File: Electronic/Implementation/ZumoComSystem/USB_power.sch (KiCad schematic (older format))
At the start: 1 part, among them P1 USB_C_Plug

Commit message: electronic -> Schematic -> add hierarchical pins, modified Regulator page
           -> BOM & Clac: add new inductors
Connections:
- net labels added: D+, D-, V_Bat
- wire segments 0 -> 2
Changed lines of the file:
@@
 L Connector:USB_C_Plug P?
 U 1 1 60C67689
-P 1400 2100
+P 1900 2100
 AR Path="/60C67689" Ref="P?"  Part="1"
 AR Path="/60C3F428/60C67689" Ref="P1"  Part="1"
-F 0 "P1" H 1507 3367 50  0000 C CNN
-F 1 "USB_C_Plug" H 1507 3276 50  0000 C CNN
-F 2 "footprints:USB_C_Receptacle_JAE_DX07S024WJ3R400" H 1550 2100 50  0001 C CNN
-F 3 "https://www.usb.org/sites/default/files/documents/usb_type-c.zip" H 1550 2100 50  0001 C CNN
-	1    1400 2100
+F 0 "P1" H 2007 3367 50  0000 C CNN
+F 1 "USB_C_Plug" H 2007 3276 50  0000 C CNN
+F 2 "footprints:USB_C_Receptacle_JAE_DX07S024WJ3R400" H 2050 2100 50  0001 C CNN
+F 3 "https://www.usb.org/sites/default/files/documents/usb_type-c.zip" H 2050 2100 50  0001 C CNN
+	1    1900 2100
 	1    0    0    -1
 $EndComp
+Text HLabel 1100 4400 0    50   Input ~ 0
+V_Bat
+Text HLabel 3050 1600 2    50   Output ~ 0
+D-
+Text HLabel 3050 1800 2    50   Output ~ 0
+D+
+Wire Wire Line
+	2500 1600 3050 1600
+Wire Wire Line
+	2500 1800 3050 1800
 $EndSCHEMATC

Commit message: Electronic: Schematic: ESP I/Os, IF_Pololu Pins, USB_max
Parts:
- removed P1: USB_C_Plug, footprints:USB_C_Receptacle_JAE_DX07S024WJ3R400, symbol Connector:USB_C_Plug
- added J2: USB_B_Micro, footprints:USB_Micro-B_Molex-105133-0001-3D, symbol Connector:USB_B_Micro
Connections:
- net labels added: GND
- wire segments 2 -> 10
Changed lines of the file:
@@
 $Descr A4 11693 8268
 encoding utf-8
-Sheet 4 7
+Sheet 5 7
 Title "Zumo Communication System"
-Date "2021-06-11"
+Date "2021-07-28"
 Rev "V1.0"
 Comp "NewTec GmbH"
@@
 Comment4 ""
 $EndDescr
+Text HLabel 2850 1450 2    50   Output ~ 0
+V_Bat
+Text HLabel 2850 1750 2    50   BiDi ~ 0
+D-
+Text HLabel 2850 1650 2    50   BiDi ~ 0
+D+
+Wire Wire Line
+	2300 1750 2850 1750
+Wire Wire Line
+	2300 1650 2850 1650
 $Comp
-L Connector:USB_C_Plug P?
-U 1 1 60C67689
-P 1900 2100
-AR Path="/60C67689" Ref="P?"  Part="1"
-AR Path="/60C3F428/60C67689" Ref="P1"  Part="1"
-F 0 "P1" H 2007 3367 50  0000 C CNN
-F 1 "USB_C_Plug" H 2007 3276 50  0000 C CNN
-F 2 "footprints:USB_C_Receptacle_JAE_DX07S024WJ3R400" H 2050 2100 50  0001 C CNN
-F 3 "https://www.usb.org/sites/default/files/documents/usb_type-c.zip" H 2050 2100 50  0001 C CNN
-	1    1900 2100
+L Connector:USB_B_Micro J2
+U 1 1 60DEC307
+P 2000 1650
+F 0 "J2" H 2057 2117 50  0000 C CNN
+F 1 "USB_B_Micro" H 2057 2026 50  0000 C CNN
+F 2 "footprints:USB_Micro-B_Molex-105133-0001-3D" H 2150 1600 50  0001 C CNN
+F 3 "~" H 2150 1600 50  0001 C CNN
+	1    2000 1650
 	1    0    0    -1
 $EndComp
-Text HLabel 1100 4400 0    50   Input ~ 0
-V_Bat
-Text HLabel 3050 1600 2    50   Output ~ 0
-D-
-Text HLabel 3050 1800 2    50   Output ~ 0
-D+
 Wire Wire Line
-	2500 1600 3050 1600
+	2850 1450 2300 1450
 Wire Wire Line
-	2500 1800 3050 1800
+	1900 2050 1900 2150
+Wire Wire Line
+	2000 2150 2000 2050
+Wire Wire Line
+	2000 2150 2000 2250
+$Comp
+L power:GND #PWR020
+U 1 1 60DEDA4E
+P 2000 2250
+F 0 "#PWR020" H 2000 2000 50  0001 C CNN
+F 1 "GND" H 2005 2077 50  0000 C CNN
+F 2 "" H 2000 2250 50  0001 C CNN
+F 3 "" H 2000 2250 50  0001 C CNN
+	1    2000 2250
+	1    0    0    -1
+$EndComp
+Wire Wire Line
+	2000 2150 2350 2150
+Wire Wire Line
+	2350 2150 2350 1850
+Wire Wire Line
+	2350 1850 2300 1850
+Connection ~ 2000 2150
+Wire Wire Line
+	1900 2150 2000 2150
 $EndSCHEMATC

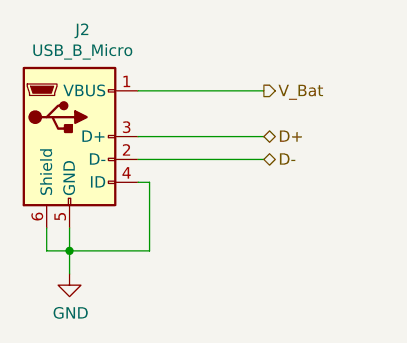
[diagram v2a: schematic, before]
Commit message: electronic: BOM: n-mosfet; SMD-pin correct position
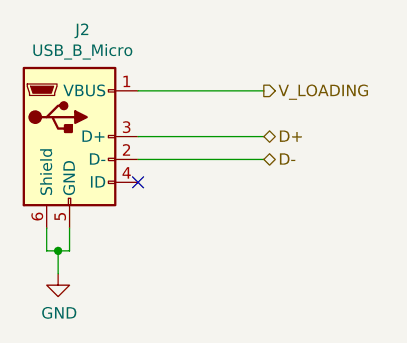
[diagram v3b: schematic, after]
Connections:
- net GND: no longer J2.4 (ID)
- net V_Bat renamed V_LOADING
- no-connect marks 0 -> 1
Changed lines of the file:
@@
 Sheet 5 7
 Title "Zumo Communication System"
-Date "2021-07-28"
+Date "2021-07-30"
 Rev "V1.0"
 Comp "NewTec GmbH"
 Comment1 "Schneider, Niklas"
-Comment2 "Schneider, Niklas"
+Comment2 ""
 Comment3 ""
 Comment4 ""
 $EndDescr
 Text HLabel 2850 1450 2    50   Output ~ 0
-V_Bat
+V_LOADING
 Text HLabel 2850 1750 2    50   BiDi ~ 0
 D-
@@
 	2000 2150 2000 2050
 Wire Wire Line
-	2000 2150 2000 2250
+	1950 2150 1950 2250
 $Comp
 L power:GND #PWR020
 U 1 1 60DEDA4E
-P 2000 2250
-F 0 "#PWR020" H 2000 2000 50  0001 C CNN
-F 1 "GND" H 2005 2077 50  0000 C CNN
-F 2 "" H 2000 2250 50  0001 C CNN
-F 3 "" H 2000 2250 50  0001 C CNN
-	1    2000 2250
+P 1950 2250
+F 0 "#PWR020" H 1950 2000 50  0001 C CNN
+F 1 "GND" H 1955 2077 50  0000 C CNN
+F 2 "" H 1950 2250 50  0001 C CNN
+F 3 "" H 1950 2250 50  0001 C CNN
+	1    1950 2250
 	1    0    0    -1
 $EndComp
 Wire Wire Line
-	2000 2150 2350 2150
+	1900 2150 1950 2150
+Connection ~ 1950 2150
 Wire Wire Line
-	2350 2150 2350 1850
-Wire Wire Line
-	2350 1850 2300 1850
-Connection ~ 2000 2150
-Wire Wire Line
-	1900 2150 2000 2150
+	1950 2150 2000 2150
+NoConn ~ 2300 1850
 $EndSCHEMATC

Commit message: add charger
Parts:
- added C?: 22uF, Capacitor_SMD:C_1206_3216Metric_Pad1.42x1.75mm_HandSolder, symbol Device:C
- added C?: 220n, symbol Device:C
- added R?: 10k, symbol Device:R
- added R?: 10, symbol Device:R
- added U?: R1218N021A, Package_TO_SOT_SMD:SOT-23-6_Handsoldering, symbol LT1374CS8-5PBF:R1218N021A
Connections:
- net GND: now also C?.2, R?.2, U?.5 (GND)
- net V_LOADING: now also C?.1, U?.2 (VOUT); no longer J2.1 (VBUS)
- new net: R?.1, U?.1 (CE)
- new net: C?.2, U?.4 (Lx)
- new net: R?.1, U?.6 (VFB)
- new net V_USB_Bat: C?.1, J2.1 (VBUS), R?.2, U?.3 (VIN)
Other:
- note added: "V_Loading = 8.5V"
- moved on the sheet: J2
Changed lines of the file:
@@
 Comment4 ""
 $EndDescr
-Text HLabel 2850 1450 2    50   Output ~ 0
+Text HLabel 6000 2350 0    50   Output ~ 0
 V_LOADING
-Text HLabel 2850 1750 2    50   BiDi ~ 0
+Text HLabel 3150 3300 2    50   BiDi ~ 0
 D-
-Text HLabel 2850 1650 2    50   BiDi ~ 0
+Text HLabel 3150 3200 2    50   BiDi ~ 0
 D+
 Wire Wire Line
-	2300 1750 2850 1750
+	2800 3300 3150 3300
 Wire Wire Line
-	2300 1650 2850 1650
+	2800 3200 3150 3200
 $Comp
 L Connector:USB_B_Micro J2
 U 1 1 60DEC307
-P 2000 1650
-F 0 "J2" H 2057 2117 50  0000 C CNN
-F 1 "USB_B_Micro" H 2057 2026 50  0000 C CNN
-F 2 "footprints:USB_Micro-B_Molex-105133-0001-3D" H 2150 1600 50  0001 C CNN
-F 3 "~" H 2150 1600 50  0001 C CNN
-	1    2000 1650
+P 2500 3200
+F 0 "J2" H 2557 3667 50  0000 C CNN
+F 1 "USB_B_Micro" H 2557 3576 50  0000 C CNN
+F 2 "footprints:USB_Micro-B_Molex-105133-0001-3D" H 2650 3150 50  0001 C CNN
+F 3 "~" H 2650 3150 50  0001 C CNN
+	1    2500 3200
 	1    0    0    -1
 $EndComp
 Wire Wire Line
-	2850 1450 2300 1450
+	2400 3600 2400 3700
 Wire Wire Line
-	1900 2050 1900 2150
+	2500 3700 2500 3600
 Wire Wire Line
-	2000 2150 2000 2050
-Wire Wire Line
-	1950 2150 1950 2250
+	2450 3700 2450 3800
 $Comp
 L power:GND #PWR020
 U 1 1 60DEDA4E
-P 1950 2250
-F 0 "#PWR020" H 1950 2000 50  0001 C CNN
-F 1 "GND" H 1955 2077 50  0000 C CNN
-F 2 "" H 1950 2250 50  0001 C CNN
-F 3 "" H 1950 2250 50  0001 C CNN
-	1    1950 2250
+P 2450 3800
+F 0 "#PWR020" H 2450 3550 50  0001 C CNN
+F 1 "GND" H 2455 3627 50  0000 C CNN
+F 2 "" H 2450 3800 50  0001 C CNN
+F 3 "" H 2450 3800 50  0001 C CNN
+	1    2450 3800
 	1    0    0    -1
 $EndComp
 Wire Wire Line
-	1900 2150 1950 2150
-Connection ~ 1950 2150
+	2400 3700 2450 3700
+Connection ~ 2450 3700
 Wire Wire Line
-	1950 2150 2000 2150
-NoConn ~ 2300 1850
+	2450 3700 2500 3700
+NoConn ~ 2800 3400
+$Comp
+L LT1374CS8-5PBF:R1218N021A U?
+U 1 1 621F5235
+P 7300 2350
+F 0 "U?" H 7300 2765 50  0000 C CNN
+F 1 "R1218N021A" H 7300 2674 50  0000 C CNN
+F 2 "Package_TO_SOT_SMD:SOT-23-6_Handsoldering" H 7700 2700 50  0001 C CNN
+F 3 "https://www.nisshinbo-microdevices.co.jp/en/pdf/datasheet/r1218-ea.pdf" H 7700 2700 50  0001 C CNN
+	1    7300 2350
+	1    0    0    -1
+$EndComp
+Wire Wire Line
+	7650 2350 8100 2350
+Wire Wire Line
+	8100 2350 8100 2750
+$Comp
+L power:GND #PWR?
+U 1 1 621F66D3
+P 8100 2750
+F 0 "#PWR?" H 8100 2500 50  0001 C CNN
+F 1 "GND" H 8105 2577 50  0000 C CNN
+F 2 "" H 8100 2750 50  0001 C CNN
+F 3 "" H 8100 2750 50  0001 C CNN
+	1    8100 2750
+	1    0    0    -1
+$EndComp
+Wire Wire Line
+	6950 2350 6250 2350
+Wire Wire Line
+	6950 2200 5800 2200
+Wire Wire Line
+	5000 3000 6800 3000
+$Comp
+L Device:R R?
+U 1 1 621FAFF2
+P 5650 2200
+F 0 "R?" V 5443 2200 50  0000 C CNN
+F 1 "10k" V 5534 2200 50  0000 C CNN
+F 2 "" V 5580 2200 50  0001 C CNN
+F 3 "~" H 5650 2200 50  0001 C CNN
+	1    5650 2200
+	0    1    1    0
+$EndComp
+Wire Wire Line
+	5500 2200 5000 2200
+$Comp
+L Device:R R?
+U 1 1 621FB991
+P 8500 2500
+F 0 "R?" H 8570 2546 50  0000 L CNN
+F 1 "10" H 8570 2455 50  0000 L CNN
+F 2 "" V 8430 2500 50  0001 C CNN
+F 3 "~" H 8500 2500 50  0001 C CNN
+	1    8500 2500
+	1    0    0    -1
+$EndComp
+Wire Wire Line
+	7650 2200 8500 2200
+$Comp
+L Device:C C?
+U 1 1 621FD3F7
+P 7300 3000
+F 0 "C?" V 7500 2950 50  0000 L CNN
+F 1 "22uF" V 7100 2900 50  0000 L CNN
+F 2 "Capacitor_SMD:C_1206_3216Metric_Pad1.42x1.75mm_HandSolder" H 7338 2850 50  0001 C CNN
+F 3 "https://product.tdk.com/info/en/catalog/datasheets/mlcc_commercial_general_en.pdf?ref_disty=digikey" H 7300 3000 50  0001 C CNN
+	1    7300 3000
+	0    -1   -1   0
+$EndComp
+Wire Wire Line
+	6800 2500 6800 3000
+Wire Wire Line
+	6800 3000 7150 3000
+Wire Wire Line
+	6800 2500 6950 2500
+Wire Wire Line
+	7450 3000 7800 3000
+Wire Wire Line
+	7800 3000 7800 2500
+Wire Wire Line
+	7800 2500 7650 2500
+Wire Wire Line
+	8500 2650 8500 2750
+$Comp
+L power:GND #PWR?
+U 1 1 621FE4AA
+P 8500 2750
+F 0 "#PWR?" H 8500 2500 50  0001 C CNN
+F 1 "GND" H 8505 2577 50  0000 C CNN
+F 2 "" H 8500 2750 50  0001 C CNN
+F 3 "" H 8500 2750 50  0001 C CNN
+	1    8500 2750
+	1    0    0    -1
+$EndComp
+Wire Wire Line
+	8500 2200 8500 2350
+Text Label 4150 3000 0    50   ~ 0
+V_USB_Bat
+Wire Wire Line
+	2800 3000 5000 3000
+Connection ~ 5000 3000
+Connection ~ 6800 3000
+Wire Wire Line
+	5000 2200 5000 3000
+$Comp
+L Device:C C?
+U 1 1 62201332
+P 6250 2550
+F 0 "C?" H 6365 2596 50  0000 L CNN
+F 1 "220n" H 6365 2505 50  0000 L CNN
+F 2 "" H 6288 2400 50  0001 C CNN
+F 3 "~" H 6250 2550 50  0001 C CNN
+	1    6250 2550
+	1    0    0    -1
+$EndComp
+Wire Wire Line
+	6250 2700 6250 2750
+Wire Wire Line
+	6250 2400 6250 2350
+Connection ~ 6250 2350
+Wire Wire Line
+	6250 2350 6000 2350
+$Comp
+L power:GND #PWR?
+U 1 1 62201F1D
+P 6250 2750
+F 0 "#PWR?" H 6250 2500 50  0001 C CNN
+F 1 "GND" H 6255 2577 50  0000 C CNN
+F 2 "" H 6250 2750 50  0001 C CNN
+F 3 "" H 6250 2750 50  0001 C CNN
+	1    6250 2750
+	1    0    0    -1
+$EndComp
+Text Notes 6950 1750 0    50   ~ 0
+V_Loading = 8.5V
 $EndSCHEMATC

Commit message: Electronic: no charger, added Cp2102 instead of Ft232, first palcement
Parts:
- removed C?: 22uF, Capacitor_SMD:C_1206_3216Metric_Pad1.42x1.75mm_HandSolder, symbol Device:C
- added D6, D7, D8: D5V0S1U2WS-7, Diode_SMD:D_SOD-323_HandSoldering, symbol Device:D
- added L3: 22uH, footprints:L_Wuerth_HCI-1350_3D, symbol Device:L
- C14: renamed from C?; footprint (none) -> Capacitor_SMD:C_0603_1608Metric_Pad1.05x0.95mm_HandSolder
- R10, R11: renamed from R?; footprint (none) -> Resistor_SMD:R_0603_1608Metric_Pad1.05x0.95mm_HandSolder
- gave numbers to parts that had none: 1
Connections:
- net D+: now also D7.1 (K)
- net D-: now also D8.1 (K)
- net GND: now also D6.2 (A), D7.2 (A), D8.2 (A)
- net at U6.4 (Lx): now also L3.2
- net V_USB_Bat renamed VBUS
- net VBUS: now also D6.1 (K), L3.1
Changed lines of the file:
@@
 Sheet 5 7
 Title "Zumo Communication System"
-Date "2021-08-20"
+Date "2022-03-08"
 Rev "V1.0"
 Comp "NewTec GmbH"
@@
 Text HLabel 6000 2350 0    50   Output ~ 0
 V_LOADING
-Text HLabel 3150 3300 2    50   BiDi ~ 0
+Text HLabel 4450 3300 2    50   BiDi ~ 0
 D-
-Text HLabel 3150 3200 2    50   BiDi ~ 0
+Text HLabel 4450 3200 2    50   BiDi ~ 0
 D+
 Wire Wire Line
-	2800 3300 3150 3300
-Wire Wire Line
-	2800 3200 3150 3200
+	2800 3300 3800 3300
+Wire Wire Line
+	2800 3200 3450 3200
 $Comp
 L Connector:USB_B_Micro J2
@@
 	2500 3700 2500 3600
 Wire Wire Line
-	2450 3700 2450 3800
-$Comp
-L power:GND #PWR020
+	2450 3700 2450 3950
+$Comp
+L power:GND #PWR030
 U 1 1 60DEDA4E
-P 2450 3800
-F 0 "#PWR020" H 2450 3550 50  0001 C CNN
-F 1 "GND" H 2455 3627 50  0000 C CNN
-F 2 "" H 2450 3800 50  0001 C CNN
-F 3 "" H 2450 3800 50  0001 C CNN
-	1    2450 3800
+P 2450 3950
+F 0 "#PWR030" H 2450 3700 50  0001 C CNN
+F 1 "GND" H 2455 3777 50  0000 C CNN
+F 2 "" H 2450 3950 50  0001 C CNN
+F 3 "" H 2450 3950 50  0001 C CNN
+	1    2450 3950
 	1    0    0    -1
 $EndComp
@@
 NoConn ~ 2800 3400
 $Comp
-L LT1374CS8-5PBF:R1218N021A U?
+L LT1374CS8-5PBF:R1218N021A U6
 U 1 1 621F5235
 P 7300 2350
-F 0 "U?" H 7300 2765 50  0000 C CNN
+F 0 "U6" H 7300 2765 50  0000 C CNN
 F 1 "R1218N021A" H 7300 2674 50  0000 C CNN
 F 2 "Package_TO_SOT_SMD:SOT-23-6_Handsoldering" H 7700 2700 50  0001 C CNN
@@
 	8100 2350 8100 2750
 $Comp
-L power:GND #PWR?
+L power:GND #PWR034
 U 1 1 621F66D3
 P 8100 2750
-F 0 "#PWR?" H 8100 2500 50  0001 C CNN
+F 0 "#PWR034" H 8100 2500 50  0001 C CNN
 F 1 "GND" H 8105 2577 50  0000 C CNN
 F 2 "" H 8100 2750 50  0001 C CNN
@@
 	5000 3000 6800 3000
 $Comp
-L Device:R R?
+L Device:R R10
 U 1 1 621FAFF2
 P 5650 2200
-F 0 "R?" V 5443 2200 50  0000 C CNN
+F 0 "R10" V 5443 2200 50  0000 C CNN
 F 1 "10k" V 5534 2200 50  0000 C CNN
-F 2 "" V 5580 2200 50  0001 C CNN
+F 2 "Resistor_SMD:R_0603_1608Metric_Pad1.05x0.95mm_HandSolder" V 5580 2200 50  0001 C CNN
 F 3 "~" H 5650 2200 50  0001 C CNN
 	1    5650 2200
@@
 	5500 2200 5000 2200
 $Comp
-L Device:R R?
+L Device:R R11
 U 1 1 621FB991
 P 8500 2500
-F 0 "R?" H 8570 2546 50  0000 L CNN
+F 0 "R11" H 8570 2546 50  0000 L CNN
 F 1 "10" H 8570 2455 50  0000 L CNN
-F 2 "" V 8430 2500 50  0001 C CNN
+F 2 "Resistor_SMD:R_0603_1608Metric_Pad1.05x0.95mm_HandSolder" V 8430 2500 50  0001 C CNN
 F 3 "~" H 8500 2500 50  0001 C CNN
 	1    8500 2500
@@
 Wire Wire Line
 	7650 2200 8500 2200
-$Comp
-L Device:C C?
-U 1 1 621FD3F7
-P 7300 3000
-F 0 "C?" V 7500 2950 50  0000 L CNN
-F 1 "22uF" V 7100 2900 50  0000 L CNN
-F 2 "Capacitor_SMD:C_1206_3216Metric_Pad1.42x1.75mm_HandSolder" H 7338 2850 50  0001 C CNN
-F 3 "https://product.tdk.com/info/en/catalog/datasheets/mlcc_commercial_general_en.pdf?ref_disty=digikey" H 7300 3000 50  0001 C CNN
-	1    7300 3000
-	0    -1   -1   0
-$EndComp
 Wire Wire Line
 	6800 2500 6800 3000
@@
 	8500 2650 8500 2750
 $Comp
-L power:GND #PWR?
+L power:GND #PWR035
 U 1 1 621FE4AA
 P 8500 2750
-F 0 "#PWR?" H 8500 2500 50  0001 C CNN
+F 0 "#PWR035" H 8500 2500 50  0001 C CNN
 F 1 "GND" H 8505 2577 50  0000 C CNN
 F 2 "" H 8500 2750 50  0001 C CNN
@@
 Wire Wire Line
 	8500 2200 8500 2350
-Text Label 4150 3000 0    50   ~ 0
-V_USB_Bat
-Wire Wire Line
-	2800 3000 5000 3000
 Connection ~ 5000 3000
 Connection ~ 6800 3000
@@
 	5000 2200 5000 3000
 $Comp
-L Device:C C?
+L Device:C C14
 U 1 1 62201332
 P 6250 2550
-F 0 "C?" H 6365 2596 50  0000 L CNN
+F 0 "C14" H 6365 2596 50  0000 L CNN
 F 1 "220n" H 6365 2505 50  0000 L CNN
-F 2 "" H 6288 2400 50  0001 C CNN
+F 2 "Capacitor_SMD:C_0603_1608Metric_Pad1.05x0.95mm_HandSolder" H 6288 2400 50  0001 C CNN
 F 3 "~" H 6250 2550 50  0001 C CNN
 	1    6250 2550
@@
 	6250 2350 6000 2350
 $Comp
-L power:GND #PWR?
+L power:GND #PWR033
 U 1 1 62201F1D
 P 6250 2750
-F 0 "#PWR?" H 6250 2500 50  0001 C CNN
+F 0 "#PWR033" H 6250 2500 50  0001 C CNN
 F 1 "GND" H 6255 2577 50  0000 C CNN
 F 2 "" H 6250 2750 50  0001 C CNN
@@
 Text Notes 6950 1750 0    50   ~ 0
 V_Loading = 8.5V
+$Comp
+L power:VBUS #PWR031
+U 1 1 6230EF27
+P 3150 2700
+F 0 "#PWR031" H 3150 2550 50  0001 C CNN
+F 1 "VBUS" H 3165 2873 50  0000 C CNN
+F 2 "" H 3150 2700 50  0001 C CNN
+F 3 "" H 3150 2700 50  0001 C CNN
+	1    3150 2700
+	1    0    0    -1
+$EndComp
+Wire Wire Line
+	3150 2700 3150 3000
+Wire Wire Line
+	2800 3000 3150 3000
+Connection ~ 3150 3000
+Wire Wire Line
+	3150 3000 5000 3000
+$Comp
+L Device:D D7
+U 1 1 6235853C
+P 3450 3600
+F 0 "D7" V 3450 3680 50  0000 L CNN
+F 1 "D5V0S1U2WS-7" V 3495 3680 50  0001 L CNN
+F 2 "Diode_SMD:D_SOD-323_HandSoldering" H 3450 3600 50  0001 C CNN
+F 3 "https://www.diodes.com/assets/Datasheets/D5V0S1U2WS.pdf" H 3450 3600 50  0001 C CNN
+	1    3450 3600
+	0    1    1    0
+$EndComp
+$Comp
+L Device:D D8
+U 1 1 62358EEE
+P 3800 3600
+F 0 "D8" V 3754 3680 50  0000 L CNN
+F 1 "D5V0S1U2WS-7" V 3800 4000 50  0000 L CNN
+F 2 "Diode_SMD:D_SOD-323_HandSoldering" H 3800 3600 50  0001 C CNN
+F 3 "https://www.diodes.com/assets/Datasheets/D5V0S1U2WS.pdf" H 3800 3600 50  0001 C CNN
+	1    3800 3600
+	0    1    1    0
+$EndComp
+Wire Wire Line
+	3450 3450 3450 3200
+Connection ~ 3450 3200
+Wire Wire Line
+	3450 3200 4450 3200
+Wire Wire Line
+	3800 3450 3800 3300
+Connection ~ 3800 3300
+Wire Wire Line
+	3800 3300 4450 3300
+$Comp
+L Device:D D6
+U 1 1 62359ADA
+P 3150 3600
+F 0 "D6" V 3150 3680 50  0000 L CNN
+F 1 "D5V0S1U2WS-7" V 3195 3680 50  0001 L CNN
+F 2 "Diode_SMD:D_SOD-323_HandSoldering" H 3150 3600 50  0001 C CNN
+F 3 "https://www.diodes.com/assets/Datasheets/D5V0S1U2WS.pdf" H 3150 3600 50  0001 C CNN
+	1    3150 3600
+	0    1    1    0
+$EndComp
+Wire Wire Line
+	3150 3450 3150 3000
+$Comp
+L power:GND #PWR032
+U 1 1 6235AC4B
+P 3450 3950
+F 0 "#PWR032" H 3450 3700 50  0001 C CNN
+F 1 "GND" H 3455 3777 50  0000 C CNN
+F 2 "" H 3450 3950 50  0001 C CNN
+F 3 "" H 3450 3950 50  0001 C CNN
+	1    3450 3950
+	1    0    0    -1
+$EndComp
+Wire Wire Line
+	3150 3750 3150 3850
+Wire Wire Line
+	3150 3850 3450 3850
+Wire Wire Line
+	3800 3850 3800 3750
+Wire Wire Line
+	3450 3750 3450 3850
+Connection ~ 3450 3850
+Wire Wire Line
+	3450 3850 3800 3850
+Wire Wire Line
+	3450 3850 3450 3950
+$Comp
+L Device:L L?
+U 1 1 623D0E3C
+P 7300 3000
+AR Path="/60C4F1BF/623D0E3C" Ref="L?"  Part="1"
+AR Path="/60C3F428/623D0E3C" Ref="L3"  Part="1"
+F 0 "L3" V 7490 3000 50  0000 C CNN
+F 1 "22uH" V 7399 3000 50  0000 C CNN
+F 2 "footprints:L_Wuerth_HCI-1350_3D" H 7300 3000 50  0001 C CNN
+F 3 "https://www.vishay.com/docs/34282/ihlp-6767gz-11.pdf" H 7300 3000 50  0001 C CNN
+	1    7300 3000
+	0    -1   -1   0
+$EndComp
 $EndSCHEMATC
